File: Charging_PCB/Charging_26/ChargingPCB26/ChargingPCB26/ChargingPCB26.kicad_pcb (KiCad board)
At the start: 2 copper layers, 100 x 100 mm, 60 parts, among them J1 Molex6pin, J2 Molex6pin, K101 Relay_SPDT_Omron_G2RL-1, K102 Relay_SPDT_Omron_G2RL-1, Q1 NMOS, Q103 Q_NPN_BEC, Q104 Q_NPN_BEC, Q105 Q_NPN_BEC, Q106 Q_NPN_BEC, Q2 NMOS, Q3 NMOS, Q4 NMOS, SW101 SW_Omron_B3FS, SW102 SW_Omron_B3FS, U1 SFH617A-1, U107 LM7805_TO220, U2 SFH617A-1, U5 74LS279, U6 74HC00

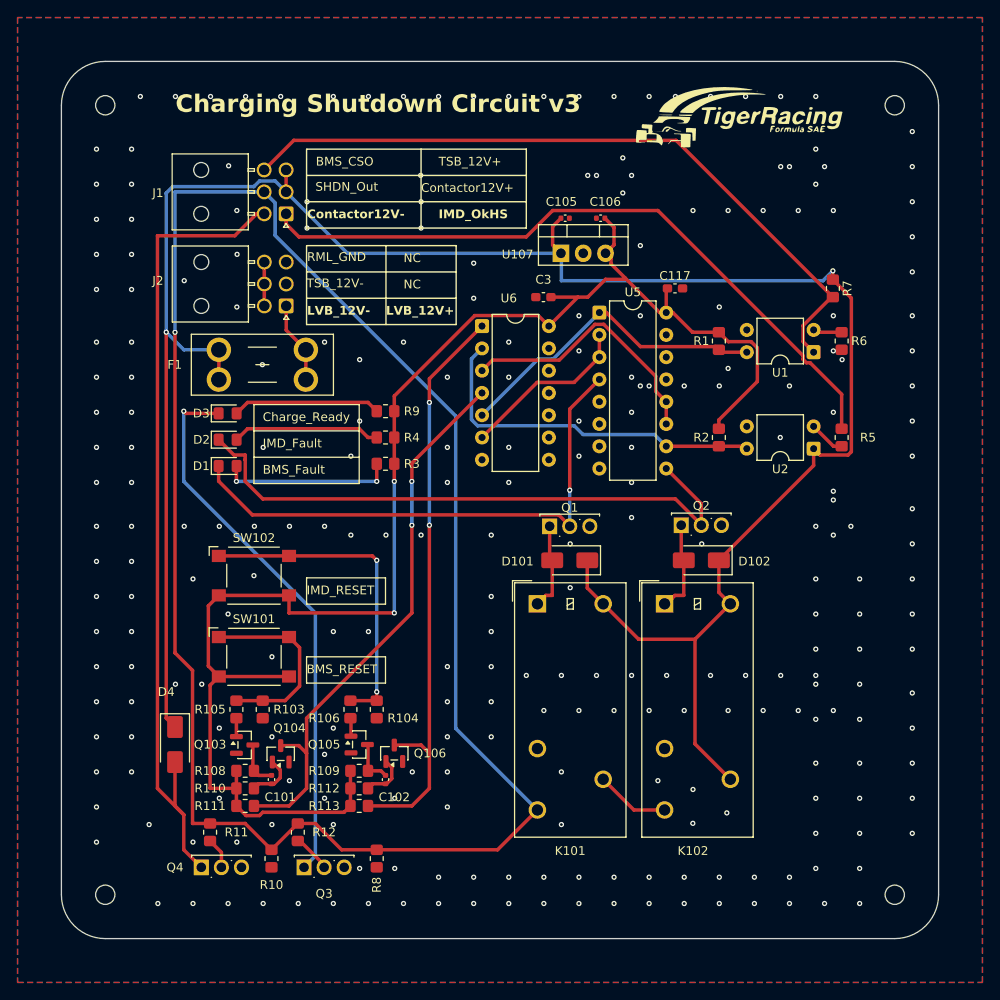
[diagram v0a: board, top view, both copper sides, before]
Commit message: charging pcb
terminated unused SR latch/Nand gate inputs
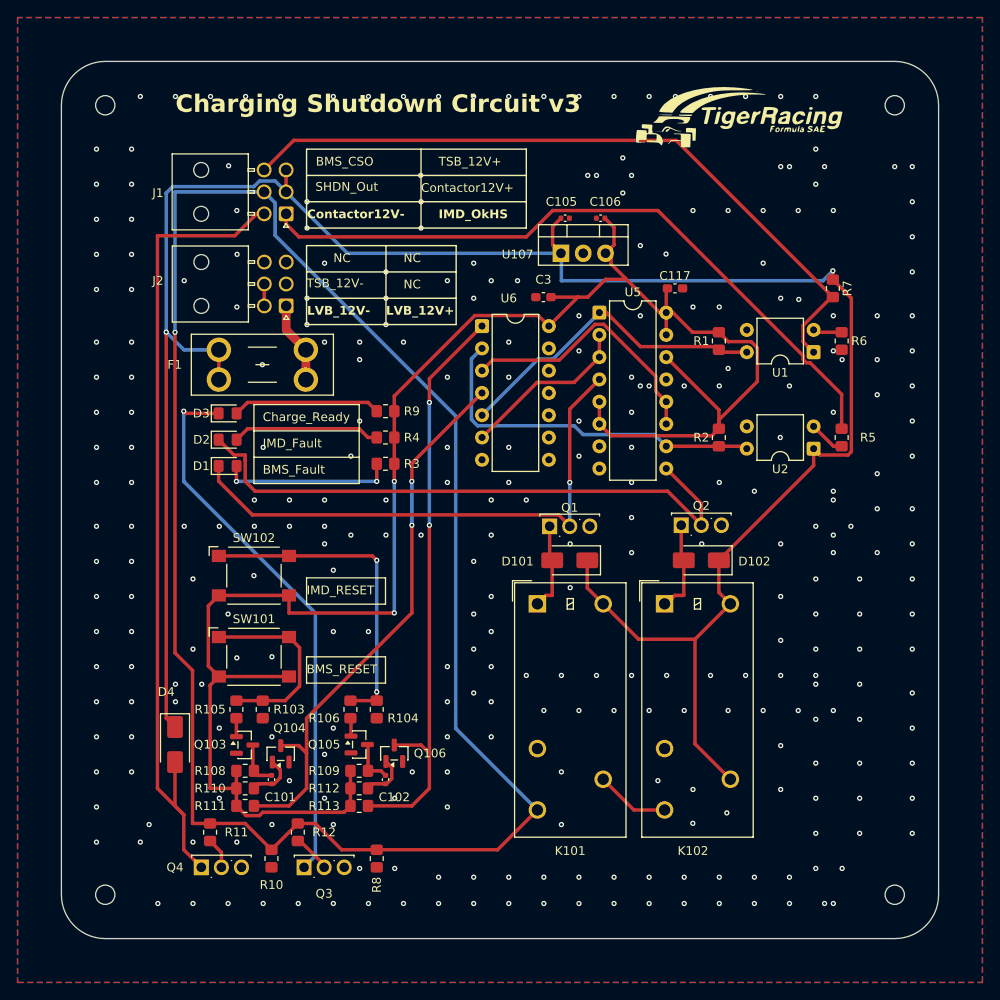
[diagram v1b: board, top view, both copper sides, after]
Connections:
- J2 pad 6: GND -> unconnected-(J2-Pin_6-Pad6)
- U5 pad 14: unconnected-(U5D-~{R}-Pad14) -> +5V
- U5 pad 15: unconnected-(U5D-~{S}-Pad15) -> +5V
- U5 pad 5: unconnected-(U5B-~{R}-Pad5) -> +5V
- U5 pad 6: unconnected-(U5B-~{S}-Pad6) -> +5V
- U6 pad 10: unconnected-(U6-Pad10) -> GND
- U6 pad 12: unconnected-(U6-Pad12) -> GND
- U6 pad 13: unconnected-(U6-Pad13) -> GND
- U6 pad 9: unconnected-(U6-Pad9) -> GND
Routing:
- net +5V: track 179.8 -> 210.0 mm
- net GND: track 5.00 -> 2.50 mm, vias 267 -> 313
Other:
- board text removed: "RML_GND"

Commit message: precharge/discharge. charging
removed discharge ffrom precharge and put it on board out of battery, updqted charging according to discharge
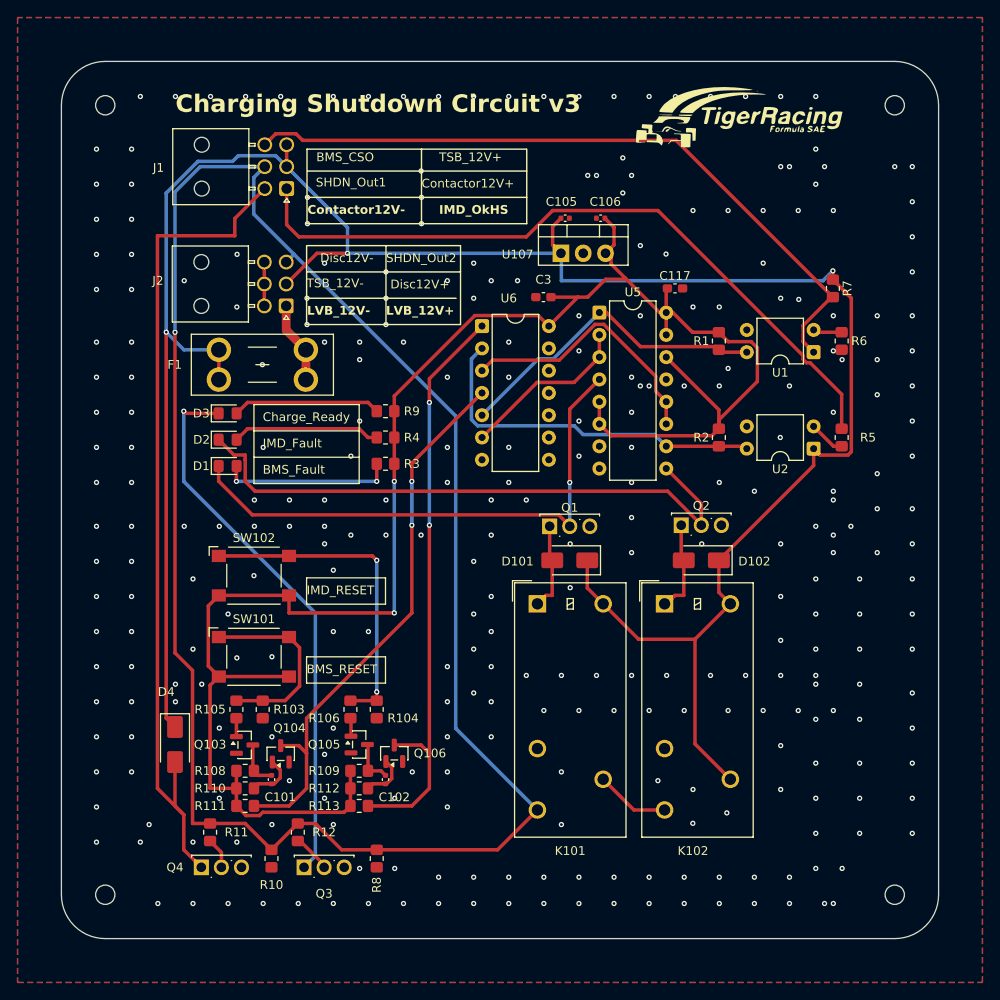
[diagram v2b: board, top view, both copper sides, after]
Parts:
- moved J1 2.88 mm to (75.7, 64.5)
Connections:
- J2 pad 2: unconnected-(J2-Pin_2-Pad2) -> +12V
- J2 pad 3: unconnected-(J2-Pin_3-Pad3) -> /Charger_SHDN
- J2 pad 6: unconnected-(J2-Pin_6-Pad6) -> GND
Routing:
- net +12V: track 252.5 -> 265.0 mm, vias 2 -> 3
- net /Charger_SHDN: track 211.3 -> 217.7 mm
- net /IMD_OKhs: track 79.2 -> 82.0 mm
- net GND: track 2.50 -> 5.00 mm, vias 313 -> 311
- net /-12V_Contactor: track 93.8 -> 96.1 mm
- net /BMS_CSO: track 81.9 -> 81.3 mm
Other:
- board text added: "Disc12V+"
- board text added: "Disc12V-"
- board text added: "SHDN_Out1"
- board text added: "SHDN_Out2"
- board text removed: "NC"
- board text removed: "SHDN_Out"

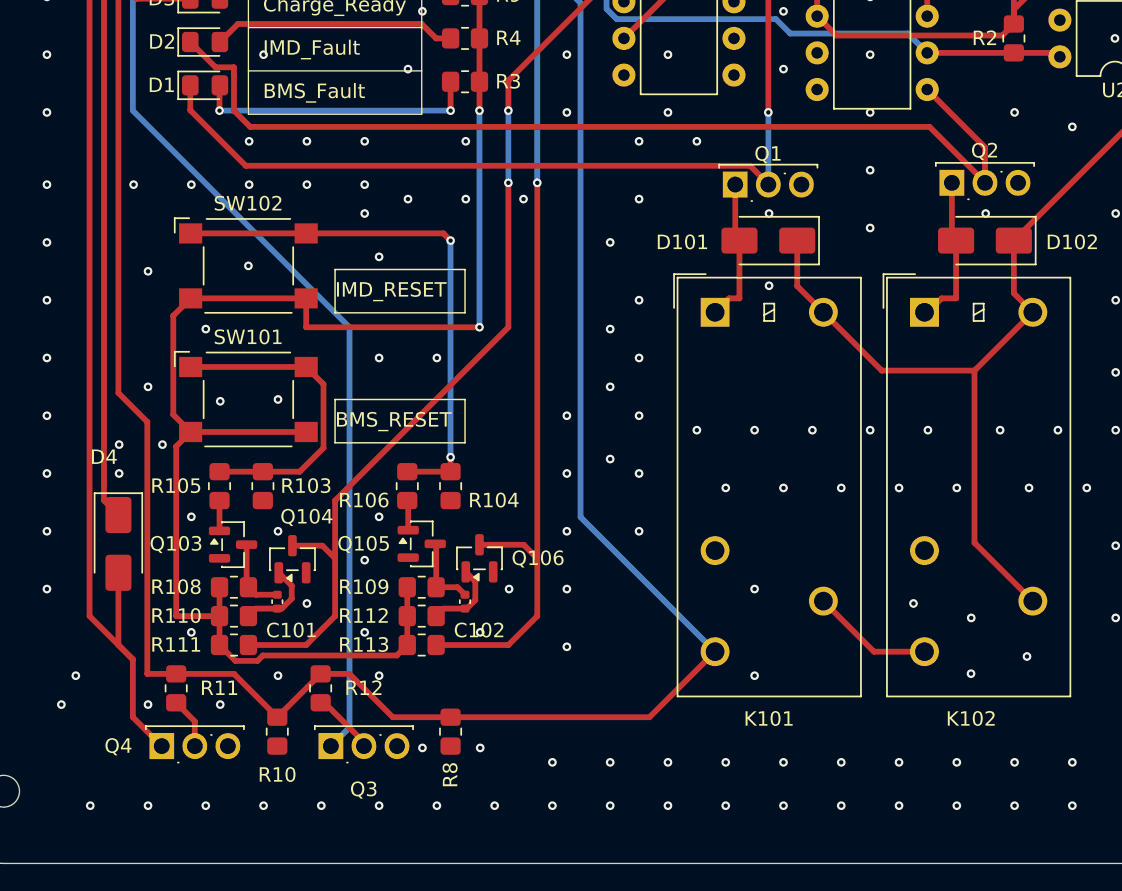
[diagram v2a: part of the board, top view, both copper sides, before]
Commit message: Charging FIxes
NMOS's Q1-4 had the wrong symbol as DGS, updated symbol and board with NMOS's Q1-4 to now have the correct symbol of GDS, to match the datasheet.
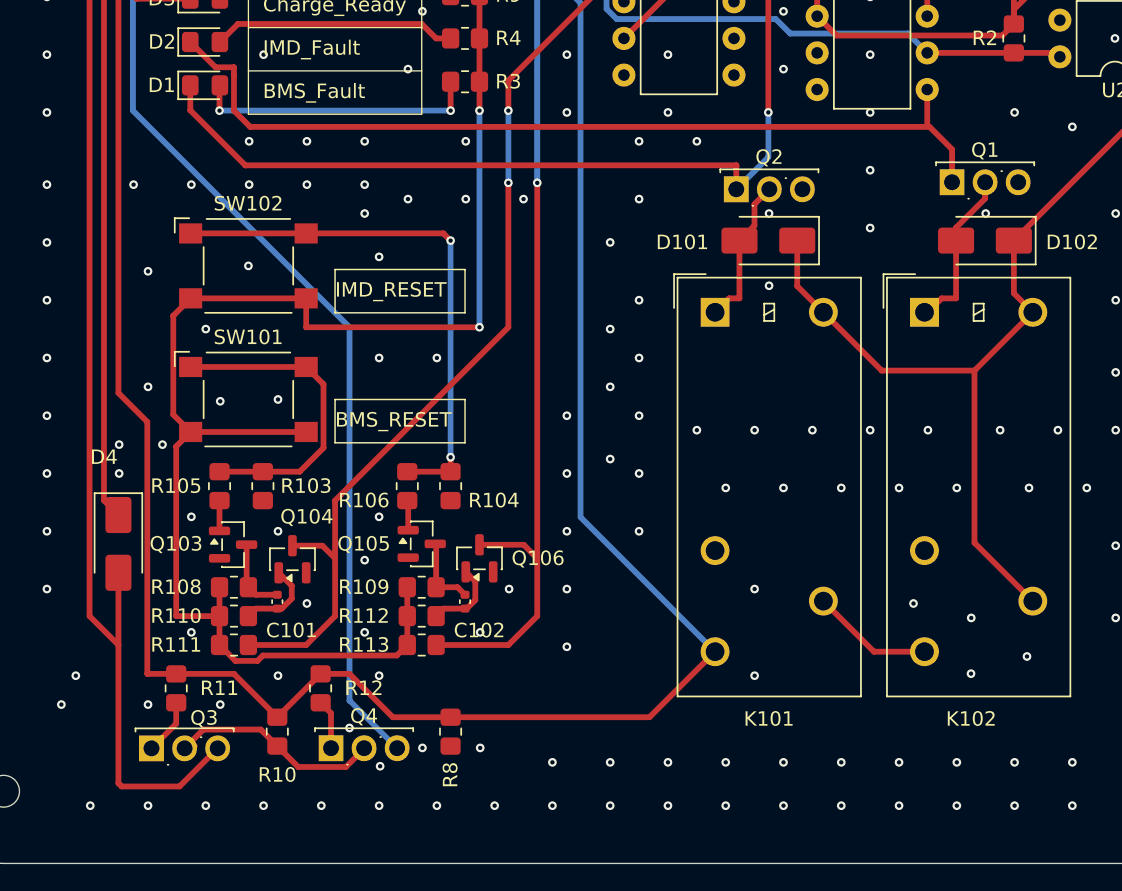
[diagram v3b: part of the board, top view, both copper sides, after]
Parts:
- D3: value LED -> LED GREEN
- Q1, Q2, Q3, Q4: value NMOS -> Q_NMOS_GDS
- moved Q1 15.0 mm to (120.7, 102.8)
- moved Q2 14.9 mm to (105.7, 103.3)
- moved Q3 12.4 mm to (65.2, 142.0)
- moved Q4 11.7 mm to (77.7, 142.0)
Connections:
- Q1 pad 1: Net-(D101-A) -> Net-(D2-K)
- Q1 pad 2: Net-(D1-K) -> Net-(D102-A)
- Q2 pad 1: Net-(D102-A) -> Net-(D1-K)
- Q2 pad 2: Net-(D2-K) -> Net-(D101-A)
- Q3 pad 1: Net-(D3-K) -> Net-(Q3-G)
- Q3 pad 2: Net-(Q3-G) -> GND
- Q3 pad 3: GND -> /-12V_Contactor
- Q4 pad 1: /-12V_Contactor -> Net-(Q4-G)
- Q4 pad 2: Net-(Q4-G) -> GND
- Q4 pad 3: GND -> Net-(D3-K)
- R11 pad 2: Net-(Q4-G) -> Net-(Q3-G)
- R12 pad 2: Net-(Q3-G) -> Net-(Q4-G)
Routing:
- net GND: track 5.00 -> 20.3 mm, vias 311 -> 313
- net /-12V_Contactor: track 96.1 -> 104.1 mm
- net Net-(D2-K): track 69.0 -> 62.5 mm
- net Net-(D102-A): track 10.7 -> 11.9 mm
- net Net-(D3-K): track 62.8 -> 63.8 mm
- net Net-(D101-A): track 10.1 -> 10.9 mm
- net Net-(Q3-G): track 4.40 -> 3.86 mm

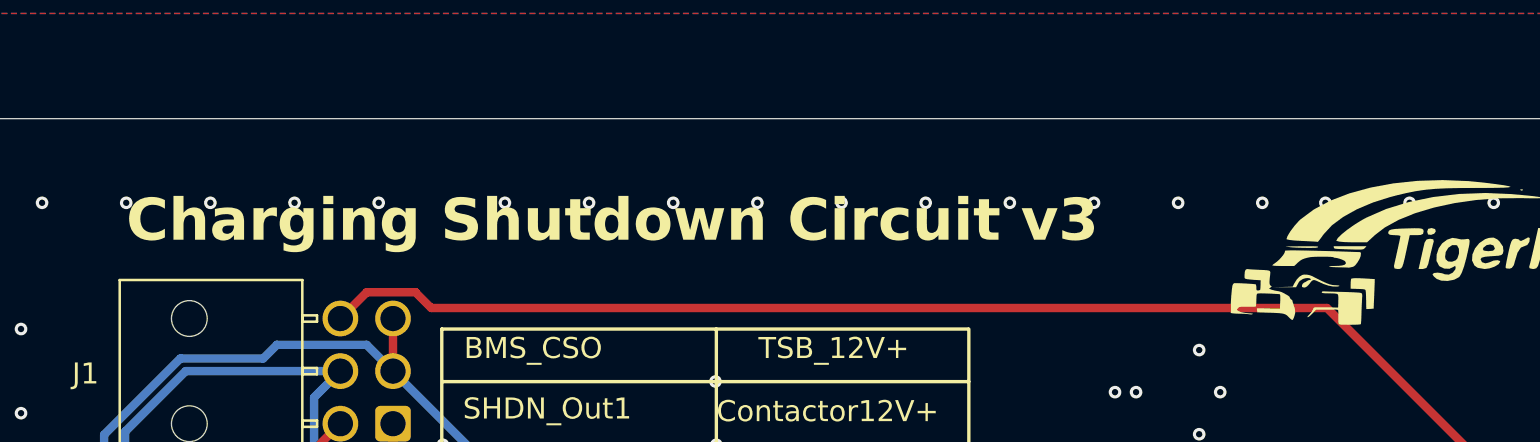
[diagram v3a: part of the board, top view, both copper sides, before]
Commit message: Discharge fixes
Fixed footprint and symbol for discharge NMOS
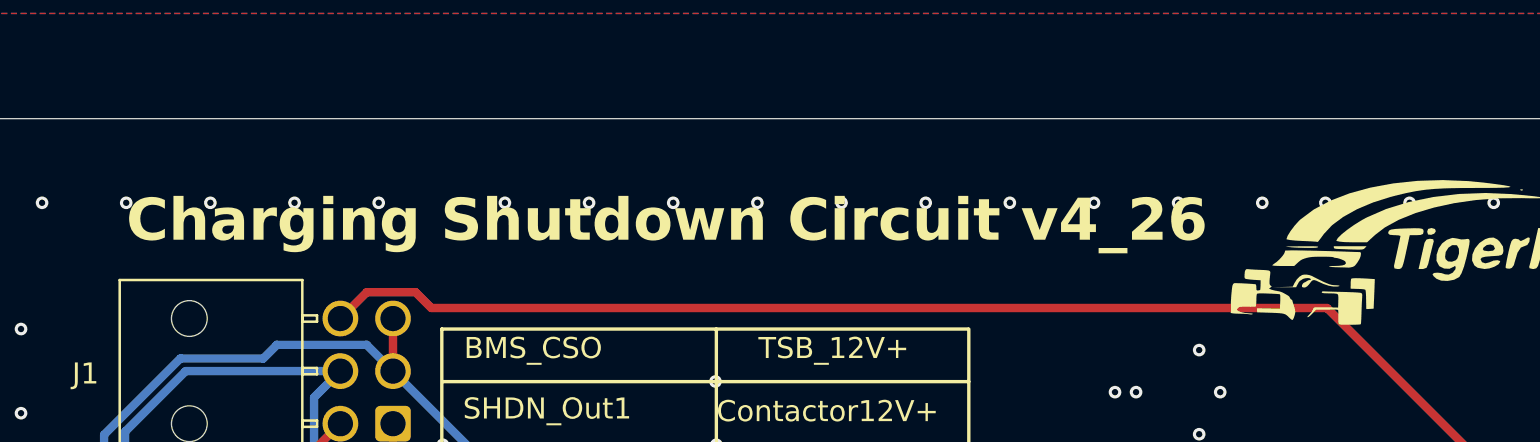
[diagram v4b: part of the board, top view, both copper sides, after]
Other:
- board text added: "Charging Shutdown Circuit v4_26"
- board text removed: "Charging Shutdown Circuit v3"
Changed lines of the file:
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@@
 		(layer "Edge.Cuts")
 	)
-	(gr_text "Charging Shutdown Circuit v3"
+	(gr_text "Charging Shutdown Circuit v4_26"
 		(at 63 56 0)
 		(layer "F.SilkS")

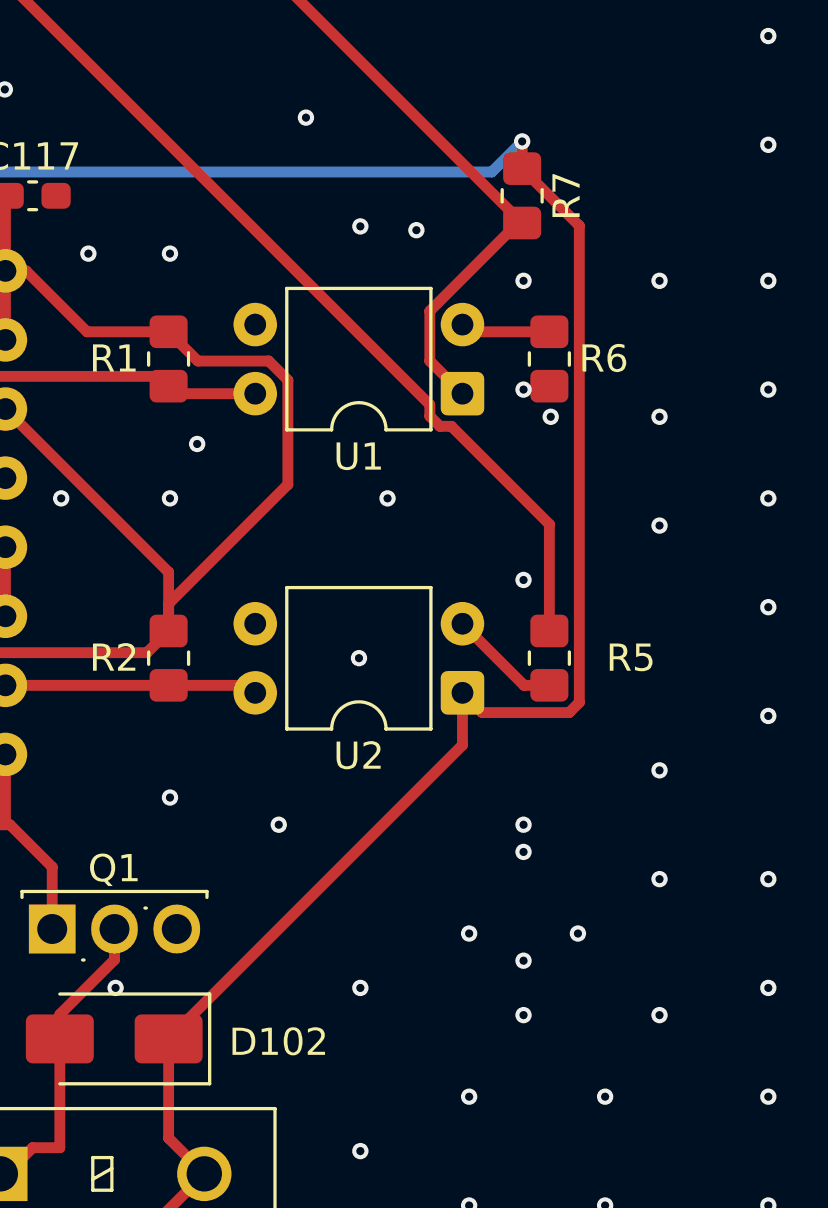
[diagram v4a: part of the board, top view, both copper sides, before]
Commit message: Charging fixes
added pull down resistor to imd signal so it faults when unconnected
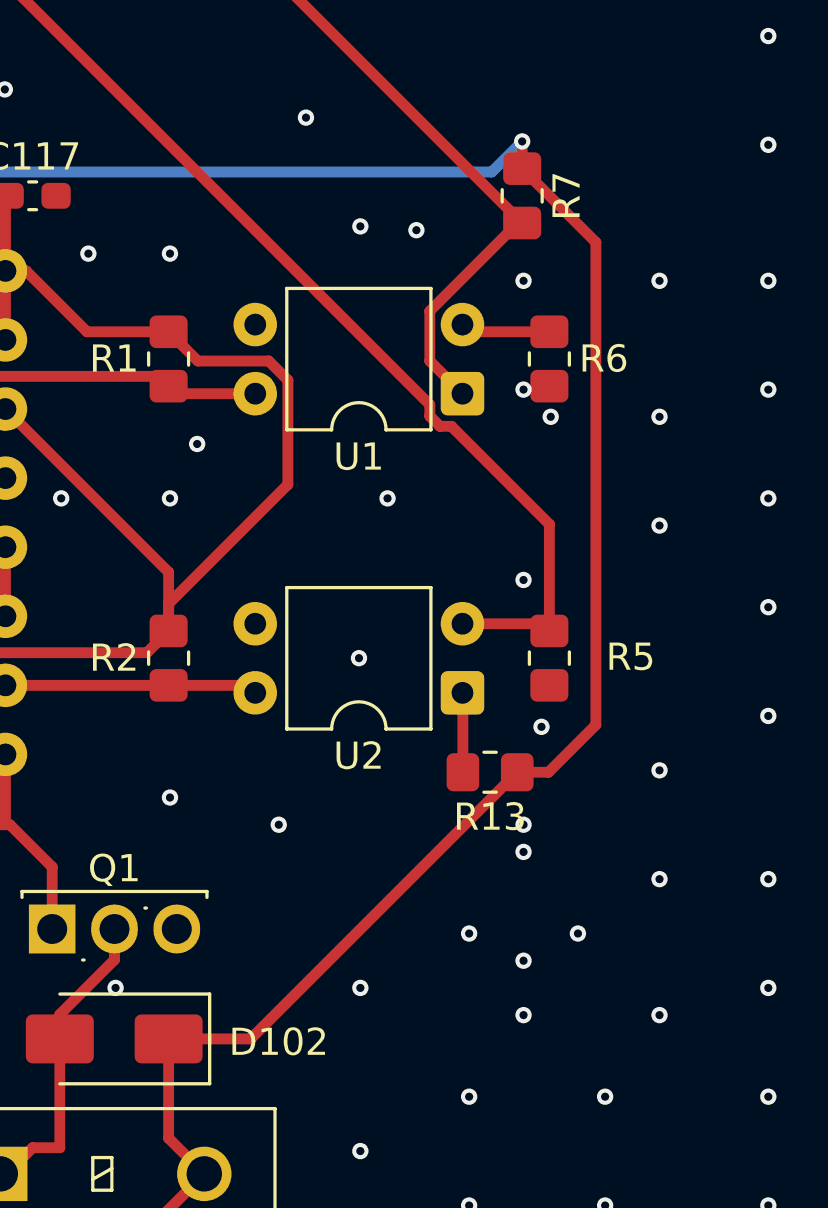
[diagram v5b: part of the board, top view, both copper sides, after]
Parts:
- added R13: 1k, Resistor_SMD:R_0805_2012Metric_Pad1.20x1.40mm_HandSolder, F.Cu at (136.8, 97.1)
- turned R5 to -90 degrees
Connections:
- R5 pad 1: Net-(R5-Pad1) -> /IMD_OKhs
- R5 pad 2: /IMD_OKhs -> GND
- U2 pad 1: +12V -> Net-(R13-Pad2)
- U2 pad 2: Net-(R5-Pad1) -> /IMD_OKhs
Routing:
- net Net-(R5-Pad1): track 4.13 -> 0.00 mm
- net /IMD_OKhs: track 82.0 -> 85.4 mm
- net Net-(R13-Pad2): track 0.00 -> 2.93 mm
- net GND: vias 313 -> 314
